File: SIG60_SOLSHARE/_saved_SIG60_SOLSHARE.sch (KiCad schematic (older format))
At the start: 66 parts, among them J1 CONN_01X05, J2 CONN_02X05, J3 CONN_01X06, J4 CONN_01X03, J5 CONN_02X04, J6 CONN_01X02, SW1 RESET, SW2 RESET, U1 SIG60, U3 ATMEGA328P-AU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

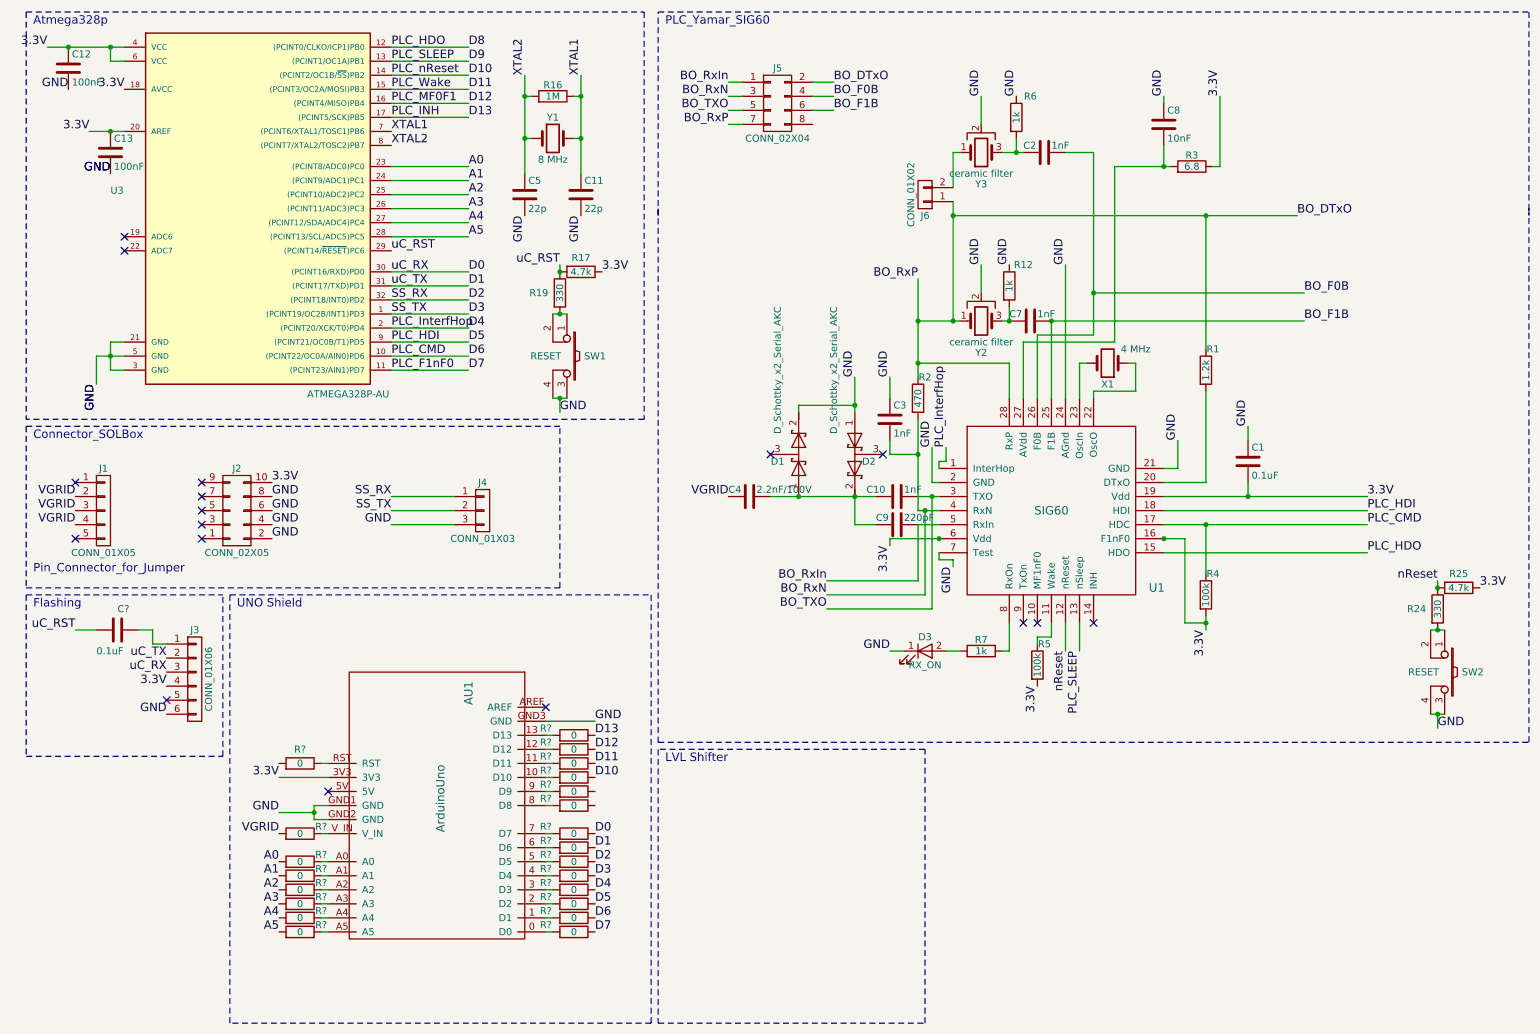
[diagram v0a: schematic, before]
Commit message: schematics changed. uno footprint added, lvl shifter added.
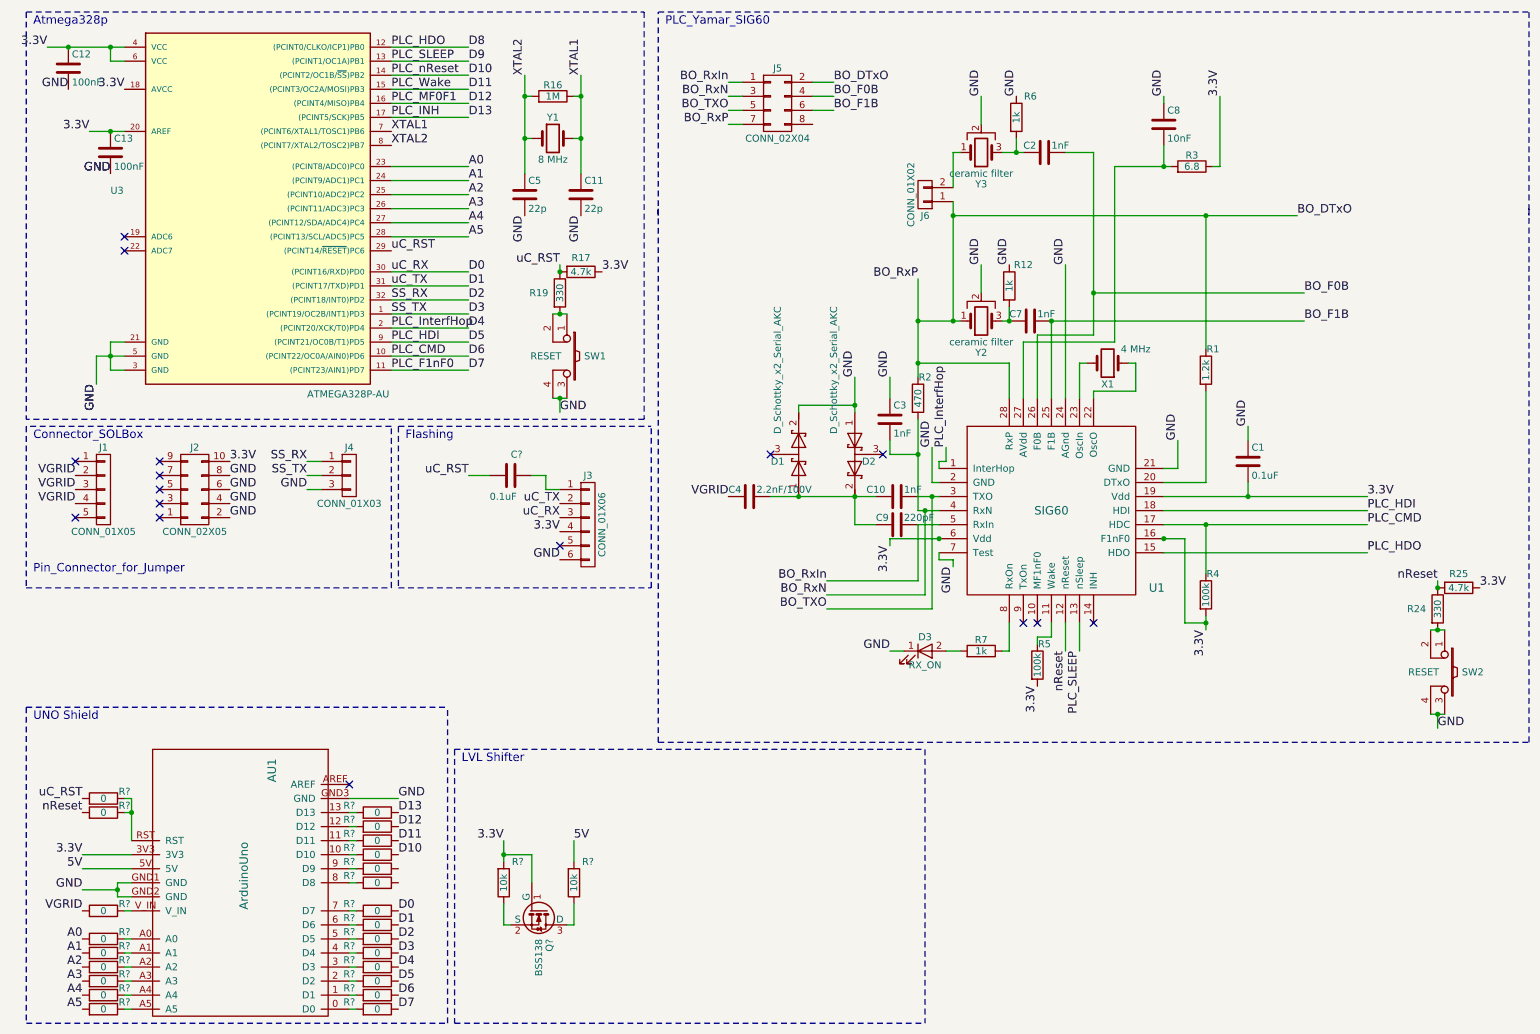
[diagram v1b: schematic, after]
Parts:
- added Q?: BSS138, TO_SOT_Packages_SMD:SOT-23, symbol BSS138
- added R? (x2): 10k, Resistors_SMD:R_0603_HandSoldering, symbol R
- added R?: 0, Resistors_SMD:R_0603_HandSoldering, symbol R
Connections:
- net 3.3V: now also Q?.1 (G), R?.2
- net nReset: now also R?.2
- net uC_RST: now also R?.2
- net 5V: now reaches AU1.5V
- net 5V: now also R?.2
- net at AU1.RST, R?.1: now also R?.1
- new net: Q?.2 (S), R?.1
- new net: Q?.3 (D), R?.1
- no-connect marks 17 -> 16
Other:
- moved on the sheet: AU1, C?, J1, J2, J3, J4, R?
